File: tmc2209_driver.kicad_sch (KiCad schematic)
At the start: 3 parts

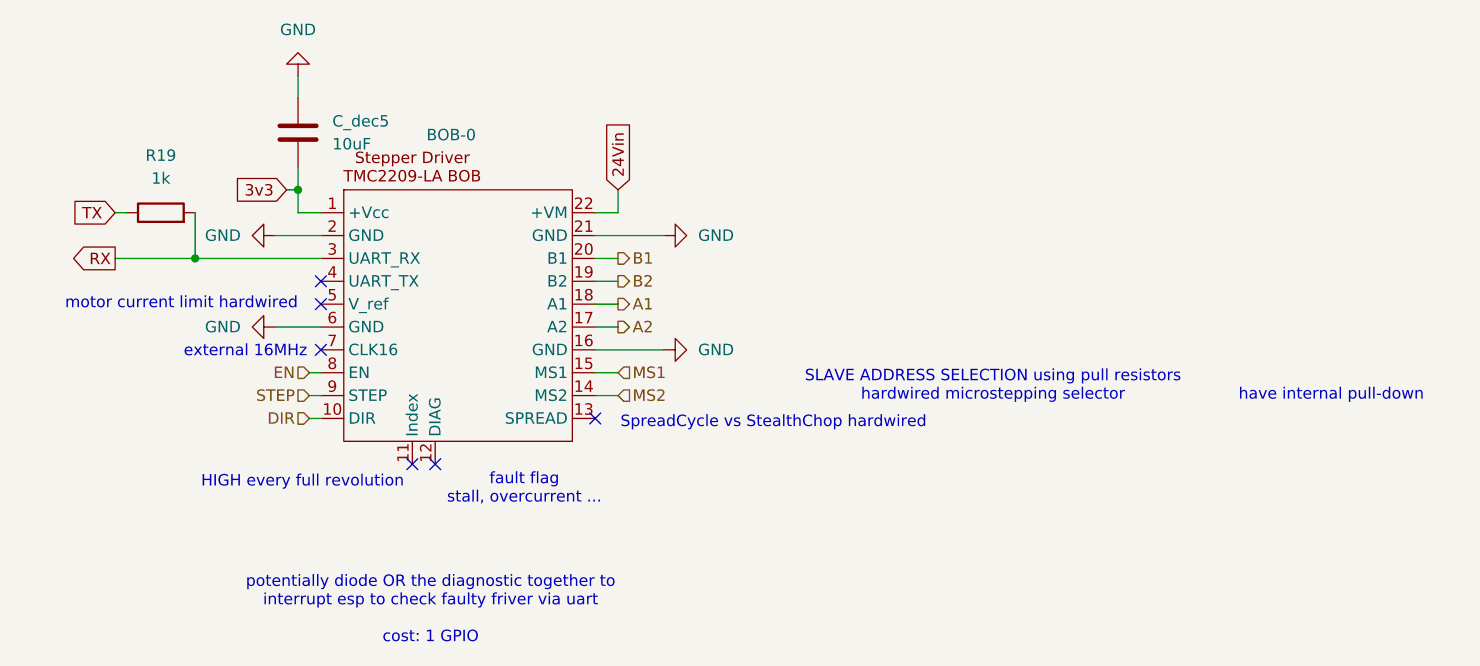
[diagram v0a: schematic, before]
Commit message: revision 1: I2C pullups, USB LDO, etc.
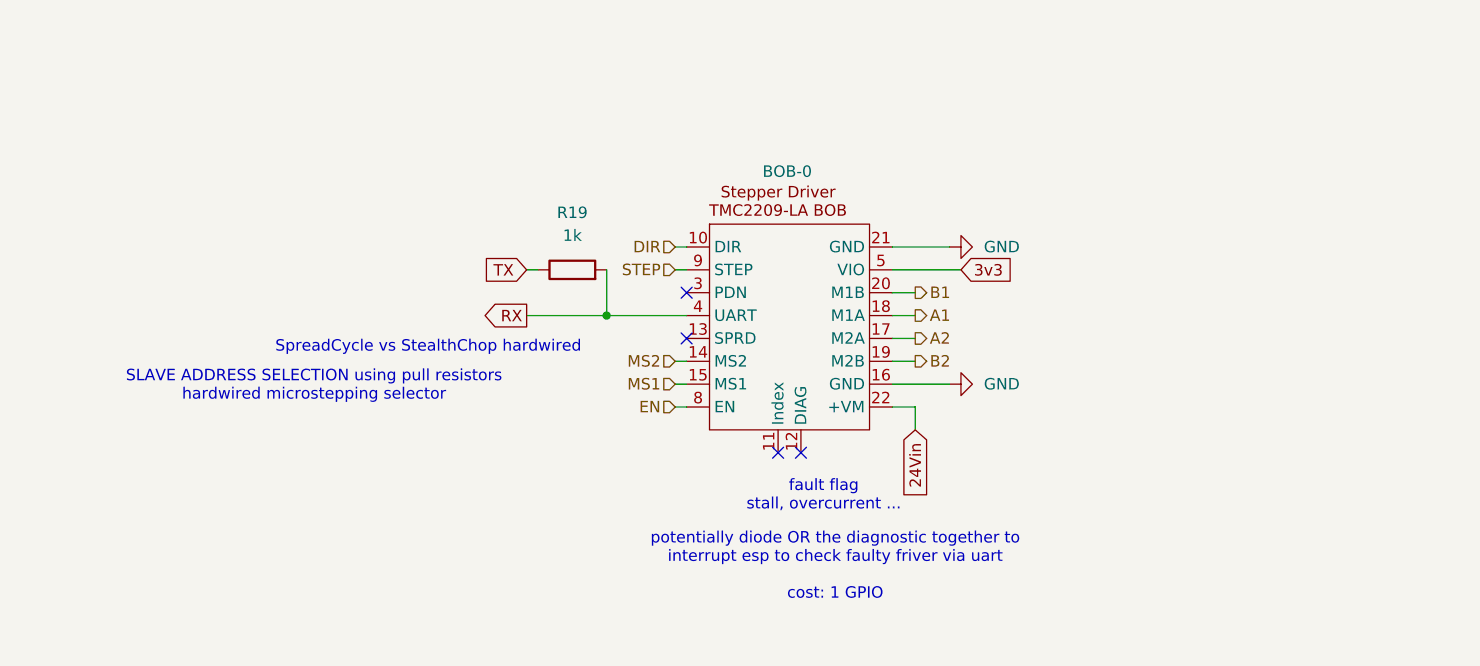
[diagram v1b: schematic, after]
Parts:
- removed C_dec5: 10uF, symbol Device:C
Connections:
- net 3v3: now also BOB-0.5 (VIO); no longer BOB-0.1 (+Vcc)
- net GND: no longer BOB-0.2 (GND), BOB-0.6 (GND)
- net RX: now also BOB-0.4 (UART); no longer BOB-0.3 (UART_RX)
- no-connect marks 6 -> 4
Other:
- note removed: "HIGH every full revolution"
- note removed: "external 16MHz"
- note removed: "have internal pull-down"
- note removed: "motor current limit hardwired"
- moved on the sheet: R19
